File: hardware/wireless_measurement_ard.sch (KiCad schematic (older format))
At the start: 24 parts, among them J1 Conn_01x08, J2 Tag-Connect, SW1 SW_SPDT, U1 EFM8LB1, U2 JDY-08, U3 MCP16415, U4 MAX40204

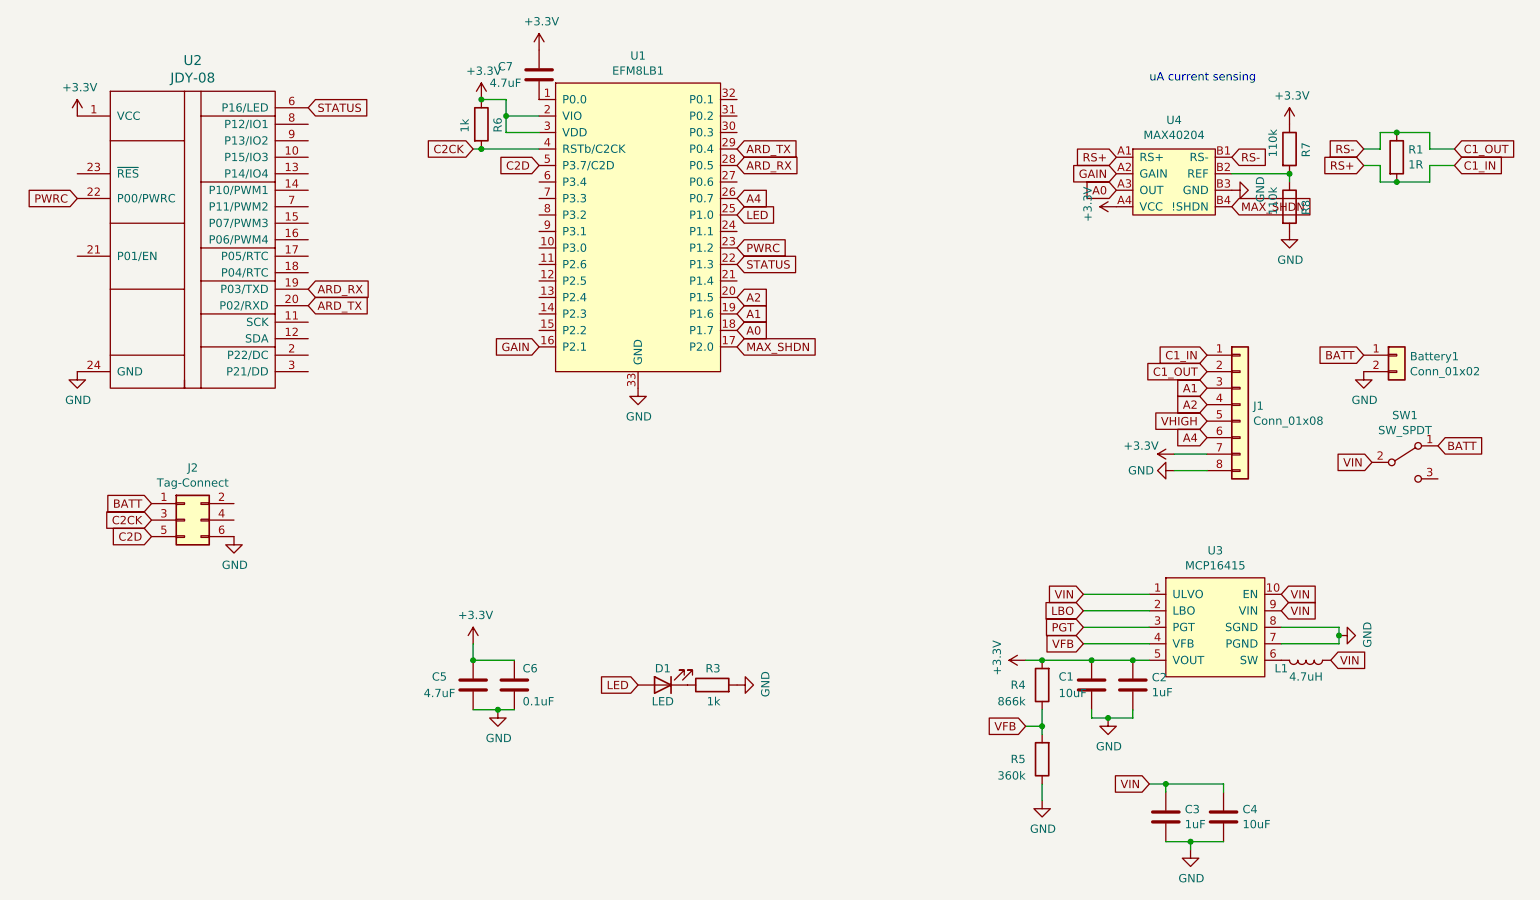
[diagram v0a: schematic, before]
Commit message: critical fix for cap connectd to power instead of gnd
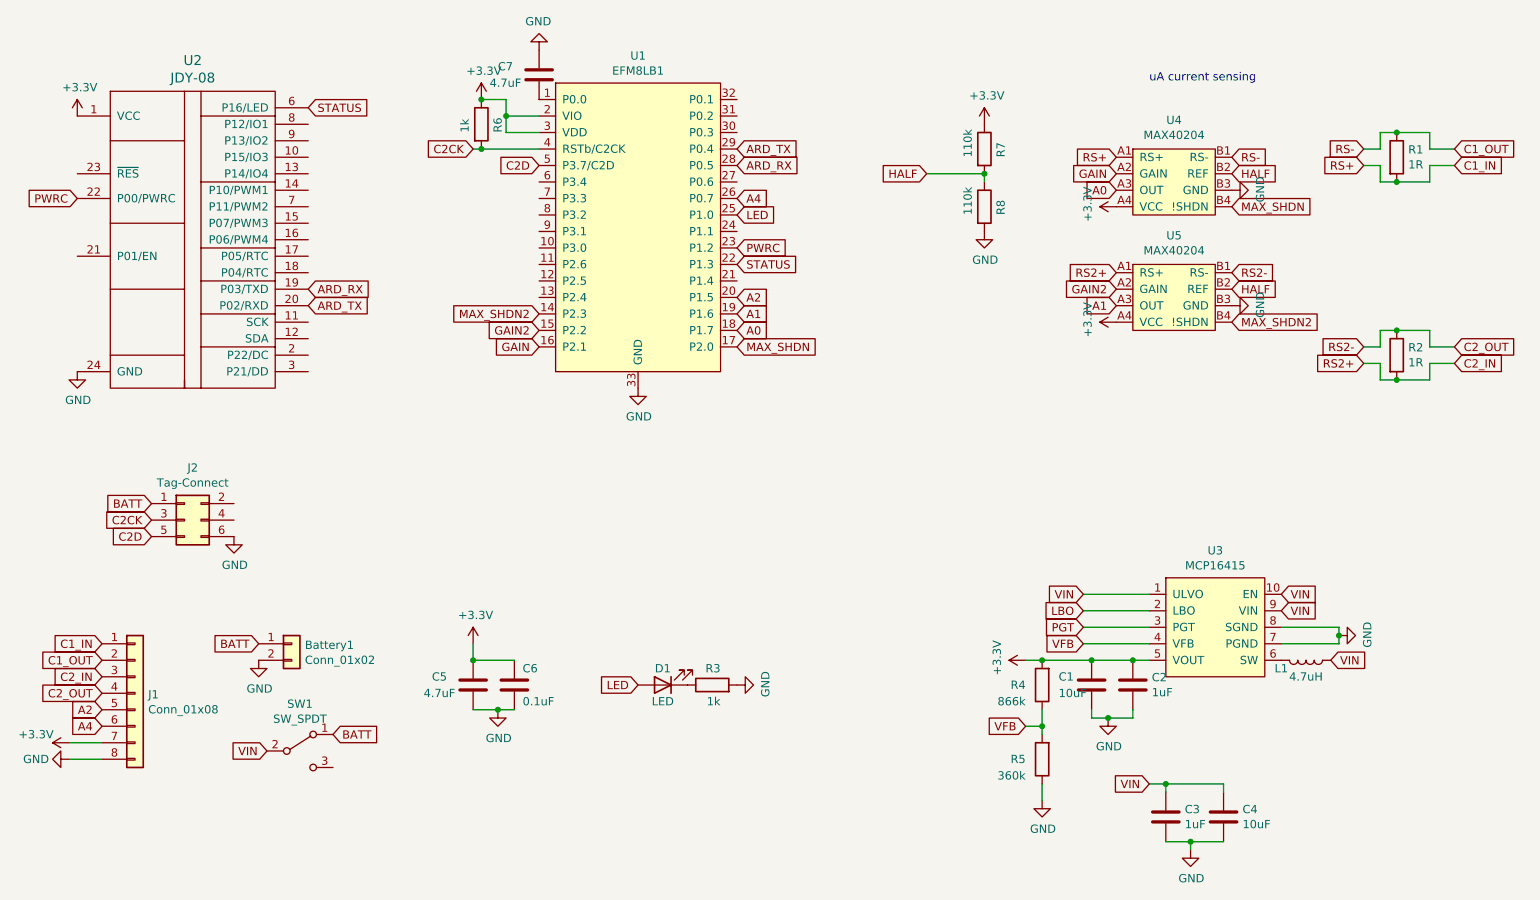
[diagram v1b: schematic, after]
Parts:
- added R2: 1R, Resistor_SMD:R_0805_2012Metric_Pad1.20x1.40mm_HandSolder, symbol Device:R
- added U5: MAX40204, ben_common:BGA-8_4x2_1.468x0.848mm, symbol ben_common:MAX40204
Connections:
- net VHIGH is gone; now on net A2: J1.5 (Pin_5)
- net +3V3: now also U5.A4 (VCC); no longer C7.1
- net A1: now also U5.A3 (OUT); no longer J1.3 (Pin_3)
- net A2: no longer J1.4 (Pin_4)
- net GND: now also C7.1, U5.B3 (GND)
- net MAX_SHDN2: now reaches U1.14 (P2.3)
- net MAX_SHDN2: now also U5.B4 (!SHDN)
- net GAIN2: now reaches U1.15 (P2.2)
- net GAIN2: now also U5.A2 (GAIN)
- net HALF: now reaches R7.2, R8.1, U4.B2 (REF)
- net HALF: now also U5.B2 (REF)
- new net C2_IN: J1.3 (Pin_3), R2.2, U5.A1 (RS+)
- new net C2_OUT: J1.4 (Pin_4), R2.1, U5.B1 (RS-)
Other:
- moved on the sheet: Battery1, J1, R7, R8, SW1

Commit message: added logo
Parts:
- added U6: Logo, icons:icon, symbol ben_common:Logo
- C1, C4: LCSC (none) -> C96446
- C2, C3: LCSC (none) -> C15849
- C5, C7: LCSC (none) -> C19666
- C6: LCSC (none) -> C14663
- R4: LCSC (none) -> C101220
- R5: LCSC (none) -> C23146
- R6: LCSC (none) -> C21190
- R7, R8: LCSC (none) -> C25805
- SW1: footprint Button_Switch_SMD:SW_SPDT_CK-JS102011SAQN -> ben_common:SW_SPDT_CK-JS102011SAQN
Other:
- moved on the sheet: C5, C6, D1, R3, R7, R8
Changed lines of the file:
@@
 F 2 "Capacitor_SMD:C_0603_1608Metric_Pad1.05x0.95mm_HandSolder" H 8638 4650 50  0001 C CNN
 F 3 "~" H 8600 4800 50  0001 C CNN
+F 4 "C96446" H 8600 4800 50  0001 C CNN "LCSC"
 	1    8600 4800
 	1    0    0    -1
@@
 F 2 "Capacitor_SMD:C_0603_1608Metric_Pad1.05x0.95mm_HandSolder" H 8888 4650 50  0001 C CNN
 F 3 "~" H 8850 4800 50  0001 C CNN
+F 4 "C15849" H 8850 4800 50  0001 C CNN "LCSC"
 	1    8850 4800
 	1    0    0    -1
@@
 F 2 "Capacitor_SMD:C_0603_1608Metric_Pad1.05x0.95mm_HandSolder" H 9088 5450 50  0001 C CNN
 F 3 "~" H 9050 5600 50  0001 C CNN
+F 4 "C15849" H 9050 5600 50  0001 C CNN "LCSC"
 	1    9050 5600
 	1    0    0    -1
@@
 F 2 "Capacitor_SMD:C_0603_1608Metric_Pad1.05x0.95mm_HandSolder" H 9438 5450 50  0001 C CNN
 F 3 "~" H 9400 5600 50  0001 C CNN
+F 4 "C96446" H 9400 5600 50  0001 C CNN "LCSC"
 	1    9400 5600
 	1    0    0    -1
@@
 F 2 "Resistor_SMD:R_0603_1608Metric_Pad1.05x0.95mm_HandSolder" V 8230 4800 50  0001 C CNN
 F 3 "~" H 8300 4800 50  0001 C CNN
+F 4 "C101220" H 8300 4800 50  0001 C CNN "LCSC"
 	1    8300 4800
 	-1   0    0    1
@@
 F 2 "Resistor_SMD:R_0603_1608Metric_Pad1.05x0.95mm_HandSolder" V 8230 5250 50  0001 C CNN
 F 3 "~" H 8300 5250 50  0001 C CNN
+F 4 "C23146" H 8300 5250 50  0001 C CNN "LCSC"
 	1    8300 5250
 	-1   0    0    1
@@
 L power:+3.3V #PWR0118
 U 1 1 6100B7A7
-P 4850 4550
-F 0 "#PWR0118" H 4850 4400 50  0001 C CNN
-F 1 "+3.3V" H 4865 4723 50  0000 C CNN
-F 2 "" H 4850 4550 50  0001 C CNN
-F 3 "" H 4850 4550 50  0001 C CNN
-	1    4850 4550
+P 5100 3450
+F 0 "#PWR0118" H 5100 3300 50  0001 C CNN
+F 1 "+3.3V" H 5115 3623 50  0000 C CNN
+F 2 "" H 5100 3450 50  0001 C CNN
+F 3 "" H 5100 3450 50  0001 C CNN
+	1    5100 3450
 	1    0    0    -1
 $EndComp
@@
 L Device:C C6
 U 1 1 610112E3
-P 5100 4800
-F 0 "C6" H 5150 4900 50  0000 L CNN
-F 1 "0.1uF" H 5150 4700 50  0000 L CNN
-F 2 "Capacitor_SMD:C_0603_1608Metric_Pad1.05x0.95mm_HandSolder" H 5138 4650 50  0001 C CNN
-F 3 "~" H 5100 4800 50  0001 C CNN
-	1    5100 4800
+P 5350 3700
+F 0 "C6" H 5400 3800 50  0000 L CNN
+F 1 "0.1uF" H 5400 3600 50  0000 L CNN
+F 2 "Capacitor_SMD:C_0603_1608Metric_Pad1.05x0.95mm_HandSolder" H 5388 3550 50  0001 C CNN
+F 3 "~" H 5350 3700 50  0001 C CNN
+F 4 "C14663" H 5350 3700 50  0001 C CNN "LCSC"
+	1    5350 3700
 	1    0    0    -1
 $EndComp
@@
 L Device:C C5
 U 1 1 61011D4D
-P 4850 4800
-F 0 "C5" H 4600 4850 50  0000 L CNN
-F 1 "4.7uF" H 4550 4750 50  0000 L CNN
-F 2 "Capacitor_SMD:C_0603_1608Metric_Pad1.05x0.95mm_HandSolder" H 4888 4650 50  0001 C CNN
-F 3 "~" H 4850 4800 50  0001 C CNN
-	1    4850 4800
-	1    0    0    -1
-$EndComp
-Wire Wire Line
-	4850 4650 4850 4550
-Wire Wire Line
-	5100 4650 4850 4650
+P 5100 3700
+F 0 "C5" H 4850 3750 50  0000 L CNN
+F 1 "4.7uF" H 4800 3650 50  0000 L CNN
+F 2 "Capacitor_SMD:C_0603_1608Metric_Pad1.05x0.95mm_HandSolder" H 5138 3550 50  0001 C CNN
+F 3 "~" H 5100 3700 50  0001 C CNN
+F 4 "C19666" H 5100 3700 50  0001 C CNN "LCSC"
+	1    5100 3700
+	1    0    0    -1
+$EndComp
+Wire Wire Line
+	5100 3550 5100 3450
+Wire Wire Line
+	5350 3550 5100 3550
 $Comp
 L power:GND #PWR0119
 U 1 1 61016AAB
-P 5000 4950
-F 0 "#PWR0119" H 5000 4700 50  0001 C CNN
-F 1 "GND" H 5005 4777 50  0000 C CNN
-F 2 "" H 5000 4950 50  0001 C CNN
-F 3 "" H 5000 4950 50  0001 C CNN
-	1    5000 4950
-	1    0    0    -1
-$EndComp
-Wire Wire Line
-	4850 4950 5000 4950
-Connection ~ 5000 4950
-Wire Wire Line
-	5000 4950 5100 4950
+P 5250 3850
+F 0 "#PWR0119" H 5250 3600 50  0001 C CNN
+F 1 "GND" H 5255 3677 50  0000 C CNN
+F 2 "" H 5250 3850 50  0001 C CNN
+F 3 "" H 5250 3850 50  0001 C CNN
+	1    5250 3850
+	1    0    0    -1
+$EndComp
+Wire Wire Line
+	5100 3850 5250 3850
+Connection ~ 5250 3850
+Wire Wire Line
+	5250 3850 5350 3850
 Text GLabel 3850 1300 2    50   Input ~ 0
 STATUS
-Connection ~ 4850 4650
+Connection ~ 5100 3550
 $Comp
 L power:GND #PWR0121
@@
 L power:GND #PWR0104
 U 1 1 61019046
-P 6450 4800
-F 0 "#PWR0104" H 6450 4550 50  0001 C CNN
-F 1 "GND" H 6455 4627 50  0000 C CNN
-F 2 "" H 6450 4800 50  0001 C CNN
-F 3 "" H 6450 4800 50  0001 C CNN
-	1    6450 4800
+P 6700 3700
+F 0 "#PWR0104" H 6700 3450 50  0001 C CNN
+F 1 "GND" H 6705 3527 50  0000 C CNN
+F 2 "" H 6700 3700 50  0001 C CNN
+F 3 "" H 6700 3700 50  0001 C CNN
+	1    6700 3700
 	0    -1   -1   0
 $EndComp
@@
 L Device:R R3
 U 1 1 6101884F
-P 6300 4800
-F 0 "R3" V 6400 4750 50  0000 L CNN
-F 1 "1k" V 6200 4750 50  0000 L CNN
-F 2 "Resistor_SMD:R_0603_1608Metric_Pad1.05x0.95mm_HandSolder" V 6230 4800 50  0001 C CNN
-F 3 "~" H 6300 4800 50  0001 C CNN
-	1    6300 4800
+P 6550 3700
+F 0 "R3" V 6650 3650 50  0000 L CNN
+F 1 "1k" V 6450 3650 50  0000 L CNN
+F 2 "Resistor_SMD:R_0603_1608Metric_Pad1.05x0.95mm_HandSolder" V 6480 3700 50  0001 C CNN
+F 3 "~" H 6550 3700 50  0001 C CNN
+	1    6550 3700
 	0    -1   -1   0
 $EndComp
@@
 L Device:LED D1
 U 1 1 61017CC7
-P 6000 4800
-F 0 "D1" H 6000 4700 50  0000 C CNN
-F 1 "LED" H 6000 4900 50  0000 C CNN
-F 2 "LED_SMD:LED_0603_1608Metric" H 6000 4800 50  0001 C CNN
-F 3 "~" H 6000 4800 50  0001 C CNN
-	1    6000 4800
+P 6250 3700
+F 0 "D1" H 6250 3600 50  0000 C CNN
+F 1 "LED" H 6250 3800 50  0000 C CNN
+F 2 "LED_SMD:LED_0603_1608Metric" H 6250 3700 50  0001 C CNN
+F 3 "~" H 6250 3700 50  0001 C CNN
+	1    6250 3700
 	-1   0    0    1
 $EndComp
-Text GLabel 5850 4800 0    50   Input ~ 0
+Text GLabel 6100 3700 0    50   Input ~ 0
 LED
 Text GLabel 6450 1950 2    50   Input ~ 0
@@
 F 2 "Resistor_SMD:R_0603_1608Metric_Pad0.98x0.95mm_HandSolder" V 4830 1400 50  0001 C CNN
 F 3 "~" H 4900 1400 50  0001 C CNN
+F 4 "C21190" V 4900 1400 50  0001 C CNN "LCSC"
 	1    4900 1400
 	1    0    0    -1
@@
 L Device:R R7
 U 1 1 6131256B
-P 7950 1550
-F 0 "R7" V 8050 1500 50  0000 L CNN
-F 1 "110k" V 7850 1500 50  0000 L CNN
-F 2 "Resistor_SMD:R_0603_1608Metric_Pad0.98x0.95mm_HandSolder" V 7880 1550 50  0001 C CNN
-F 3 "~" H 7950 1550 50  0001 C CNN
-	1    7950 1550
+P 8250 1900
+F 0 "R7" V 8350 1850 50  0000 L CNN
+F 1 "110k" V 8150 1850 50  0000 L CNN
+F 2 "Resistor_SMD:R_0603_1608Metric_Pad0.98x0.95mm_HandSolder" V 8180 1900 50  0001 C CNN
+F 3 "~" H 8250 1900 50  0001 C CNN
+F 4 "C25805" V 8250 1900 50  0001 C CNN "LCSC"
+	1    8250 1900
 	1    0    0    -1
 $EndComp
@@
 F 2 "Capacitor_SMD:C_0603_1608Metric_Pad1.08x0.95mm_HandSolder" H 5288 950 50  0001 C CNN
 F 3 "~" H 5250 1100 50  0001 C CNN
+F 4 "C19666" H 5250 1100 50  0001 C CNN "LCSC"
 	1    5250 1100
 	1    0    0    -1
@@
 L power:+3.3V #PWR0111
 U 1 1 615A4E84
-P 7950 1400
-F 0 "#PWR0111" H 7950 1250 50  0001 C CNN
-F 1 "+3.3V" H 7965 1573 50  0000 C CNN
-F 2 "" H 7950 1400 50  0001 C CNN
-F 3 "" H 7950 1400 50  0001 C CNN
-	1    7950 1400
+P 8250 1750
+F 0 "#PWR0111" H 8250 1600 50  0001 C CNN
+F 1 "+3.3V" H 8265 1923 50  0000 C CNN
+F 2 "" H 8250 1750 50  0001 C CNN
+F 3 "" H 8250 1750 50  0001 C CNN
+	1    8250 1750
 	1    0    0    -1
 $EndComp
@@
 L power:GND #PWR0120
 U 1 1 615A53CD
-P 7950 2050
-F 0 "#PWR0120" H 7950 1800 50  0001 C CNN
-F 1 "GND" H 7955 1877 50  0000 C CNN
-F 2 "" H 7950 2050 50  0001 C CNN
-F 3 "" H 7950 2050 50  0001 C CNN
-	1    7950 2050
+P 8250 2400
+F 0 "#PWR0120" H 8250 2150 50  0001 C CNN
+F 1 "GND" H 8255 2227 50  0000 C CNN
+F 2 "" H 8250 2400 50  0001 C CNN
+F 3 "" H 8250 2400 50  0001 C CNN
+	1    8250 2400
 	1    0    0    -1
 $EndComp
@@
 RS-
 Wire Wire Line
-	7950 1750 7950 1700
+	8250 2100 8250 2050
 Text GLabel 10250 1650 0    50   Input ~ 0
 RS+
@@
 $EndComp
 Wire Wire Line
-	7600 1700 7950 1700
-Connection ~ 7950 1700
+	7900 2050 8250 2050
+Connection ~ 8250 2050
 Text GLabel 2600 5050 0    50   Input ~ 0
 A4
@@
 F 0 "SW1" H 3800 5485 50  0000 C CNN
 F 1 "SW_SPDT" H 3800 5394 50  0000 C CNN
-F 2 "Button_Switch_SMD:SW_SPDT_CK-JS102011SAQN" H 3800 5200 50  0001 C CNN
+F 2 "ben_common:SW_SPDT_CK-JS102011SAQN" H 3800 5200 50  0001 C CNN
 F 3 "~" H 3800 5200 50  0001 C CNN
 	1    3800 5200
@@
 	1    0    0    -1
 $EndComp
-Text GLabel 7600 1700 0    50   Input ~ 0
+Text GLabel 7900 2050 0    50   Input ~ 0
 HALF
 $Comp
 L Device:R R8
 U 1 1 61316095
-P 7950 1900
-F 0 "R8" V 8050 1850 50  0000 L CNN
-F 1 "110k" V 7850 1850 50  0000 L CNN
-F 2 "Resistor_SMD:R_0603_1608Metric_Pad0.98x0.95mm_HandSolder" V 7880 1900 50  0001 C CNN
-F 3 "~" H 7950 1900 50  0001 C CNN
-	1    7950 1900
+P 8250 2250
+F 0 "R8" V 8350 2200 50  0000 L CNN
+F 1 "110k" V 8150 2200 50  0000 L CNN
+F 2 "Resistor_SMD:R_0603_1608Metric_Pad0.98x0.95mm_HandSolder" V 8180 2250 50  0001 C CNN
+F 3 "~" H 8250 2250 50  0001 C CNN
+F 4 "C25805" V 8250 2250 50  0001 C CNN "LCSC"
+	1    8250 2250
 	1    0    0    -1
 $EndComp
@@
 MAX_SHDN2
 $Comp
-L power:GND #PWR?
+L power:GND #PWR0102
 U 1 1 616FC7EB
 P 5250 950
-F 0 "#PWR?" H 5250 700 50  0001 C CNN
+F 0 "#PWR0102" H 5250 700 50  0001 C CNN
 F 1 "GND" H 5255 777 50  0000 C CNN
 F 2 "" H 5250 950 50  0001 C CNN
@@
 	-1   0    0    1
 $EndComp
+$Comp
+L ben_common:Logo U6
+U 1 1 615ED4AF
+P 6250 850
+F 0 "U6" H 6378 871 50  0000 L CNN
+F 1 "Logo" H 6378 780 50  0000 L CNN
+F 2 "icons:icon" H 6250 850 50  0001 C CNN
+F 3 "" H 6250 850 50  0001 C CNN
+	1    6250 850
+	1    0    0    -1
+$EndComp
 $EndSCHEMATC

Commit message: update PCB
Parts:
- added C8: 4.7uF, Capacitor_SMD:C_0603_1608Metric_Pad1.08x0.95mm_HandSolder, symbol Device:C
- added C9: 0.1uF, Capacitor_SMD:C_0603_1608Metric_Pad1.08x0.95mm_HandSolder, symbol Device:C
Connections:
- net +3V3: now also C8.1, C9.1
- net GND: now also C8.2, C9.2
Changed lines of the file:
@@
 	1    0    0    -1
 $EndComp
+$Comp
+L power:+3.3V #PWR0124
+U 1 1 6178870C
+P 8800 3150
+F 0 "#PWR0124" H 8800 3000 50  0001 C CNN
+F 1 "+3.3V" H 8815 3323 50  0000 C CNN
+F 2 "" H 8800 3150 50  0001 C CNN
+F 3 "" H 8800 3150 50  0001 C CNN
+	1    8800 3150
+	1    0    0    -1
+$EndComp
+$Comp
+L Device:C C9
+U 1 1 61788713
+P 9050 3400
+F 0 "C9" H 9100 3500 50  0000 L CNN
+F 1 "0.1uF" H 9100 3300 50  0000 L CNN
+F 2 "Capacitor_SMD:C_0603_1608Metric_Pad1.08x0.95mm_HandSolder" H 9088 3250 50  0001 C CNN
+F 3 "~" H 9050 3400 50  0001 C CNN
+F 4 "C14663" H 9050 3400 50  0001 C CNN "LCSC"
+	1    9050 3400
+	1    0    0    -1
+$EndComp
+$Comp
+L Device:C C8
+U 1 1 6178871A
+P 8800 3400
+F 0 "C8" H 8550 3450 50  0000 L CNN
+F 1 "4.7uF" H 8500 3350 50  0000 L CNN
+F 2 "Capacitor_SMD:C_0603_1608Metric_Pad1.08x0.95mm_HandSolder" H 8838 3250 50  0001 C CNN
+F 3 "~" H 8800 3400 50  0001 C CNN
+F 4 "C19666" H 8800 3400 50  0001 C CNN "LCSC"
+	1    8800 3400
+	1    0    0    -1
+$EndComp
+Wire Wire Line
+	8800 3250 8800 3150
+Wire Wire Line
+	9050 3250 8800 3250
+$Comp
+L power:GND #PWR0125
+U 1 1 61788722
+P 8950 3550
+F 0 "#PWR0125" H 8950 3300 50  0001 C CNN
+F 1 "GND" H 8955 3377 50  0000 C CNN
+F 2 "" H 8950 3550 50  0001 C CNN
+F 3 "" H 8950 3550 50  0001 C CNN
+	1    8950 3550
+	1    0    0    -1
+$EndComp
+Wire Wire Line
+	8800 3550 8950 3550
+Connection ~ 8950 3550
+Wire Wire Line
+	8950 3550 9050 3550
+Connection ~ 8800 3250
 $EndSCHEMATC

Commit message: added line to measure the half voltage for the MAX40204
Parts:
- U4, U5: symbol ben_common:MAX40204 -> wireless_measurement_ard-rescue:MAX40204-ben_common
- U6: symbol ben_common:Logo -> wireless_measurement_ard-rescue:Logo-ben_common
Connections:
- net HALF is gone; now on net A5: R7.2, R8.1, U4.B2 (REF), U5.B2 (REF)
- net A5: now reaches U1.21 (P1.4)
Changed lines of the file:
@@
 A0
 $Comp
-L ben_common:MAX40204 U4
+L wireless_measurement_ard-rescue:MAX40204-ben_common U4
 U 1 1 61604BD6
 P 9100 1750
@@
 $EndComp
 Wire Wire Line
-	7900 2050 8250 2050
+	7900 2050 8050 2050
 Connection ~ 8250 2050
 Text GLabel 2600 5050 0    50   Input ~ 0
@@
 GAIN2
 $Comp
-L ben_common:MAX40204 U5
+L wireless_measurement_ard-rescue:MAX40204-ben_common U5
 U 1 1 616414F4
 P 9100 2450
@@
 $EndComp
 $Comp
-L ben_common:Logo U6
+L wireless_measurement_ard-rescue:Logo-ben_common U6
 U 1 1 615ED4AF
 P 6250 850
@@
 	8950 3550 9050 3550
 Connection ~ 8800 3250
+Text GLabel 7900 1850 0    50   Input ~ 0
+A5
+Wire Wire Line
+	8050 2050 8050 1850
+Wire Wire Line
+	8050 1850 7900 1850
+Connection ~ 8050 2050
+Wire Wire Line
+	8050 2050 8250 2050
+Text GLabel 6450 2350 2    50   Input ~ 0
+A5
 $EndSCHEMATC
